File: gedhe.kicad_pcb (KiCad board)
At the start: 2 copper layers, 140 x 120.6 mm, 56 parts, among them SW1 switch, SW10 switch, SW11 switch, SW12 switch, SW13 switch, SW14 switch, SW15 switch, SW16 switch, SW17 switch, SW18 switch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

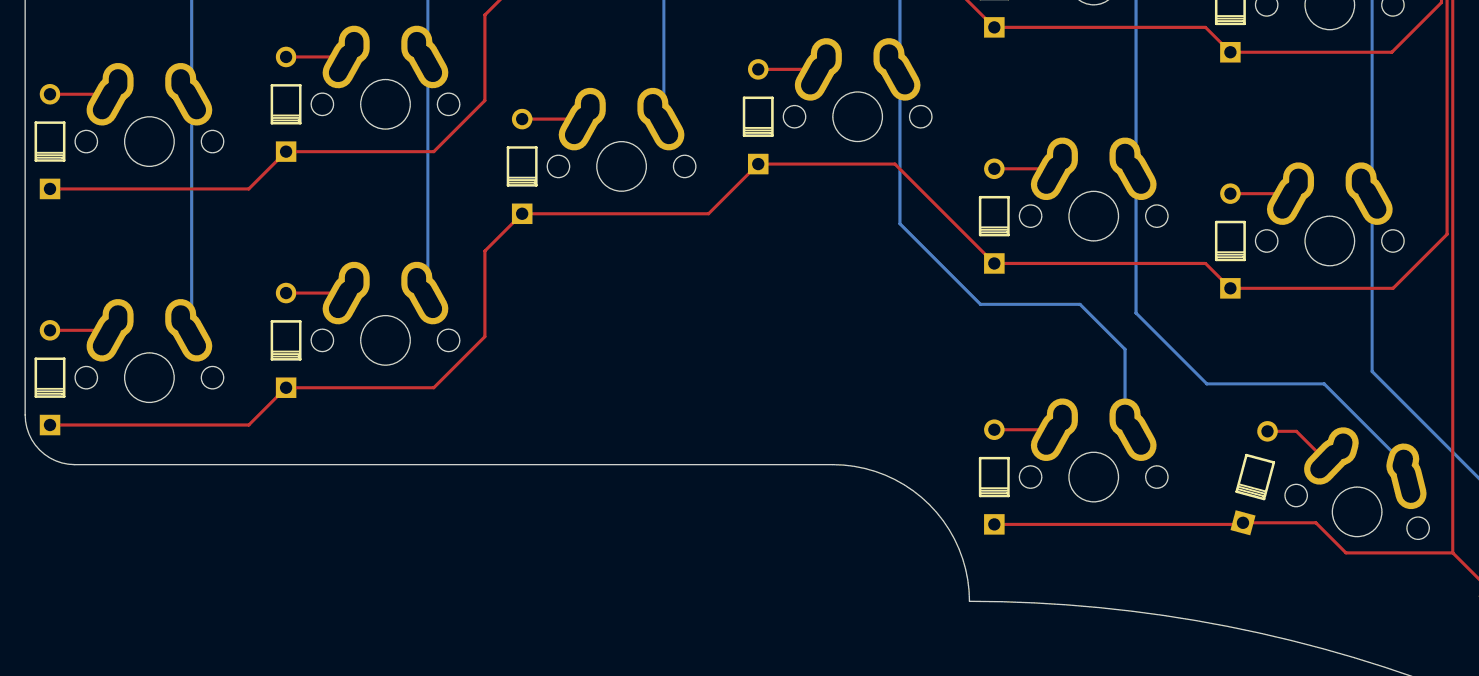
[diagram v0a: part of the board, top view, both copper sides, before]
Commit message: 29 keys per side.
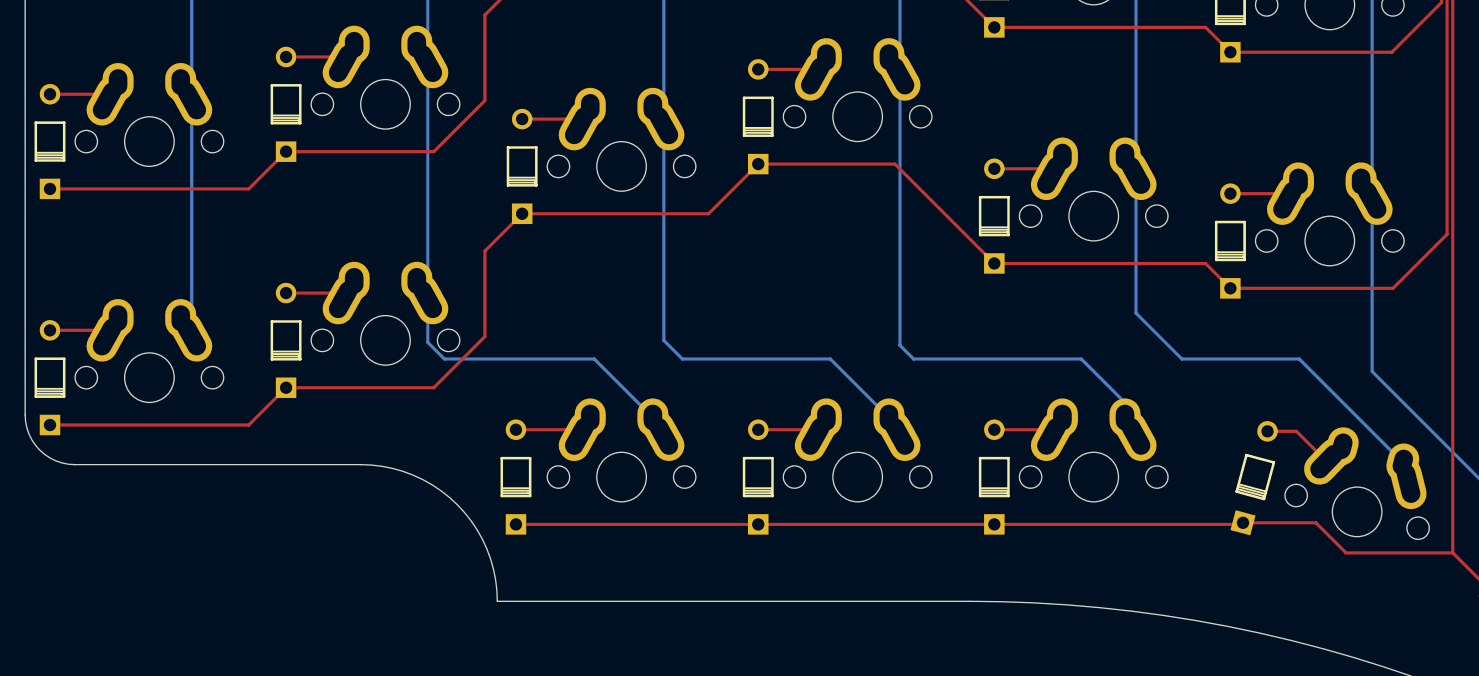
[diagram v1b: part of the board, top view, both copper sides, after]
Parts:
- added D28: D, footprints:diode, F.Cu at (62.5, 117.0)
- added D29: D, footprints:diode, F.Cu at (82.0, 117.0)
- added SW28: switch, footprints:1u-dual, F.Cu at (71.0, 117.0)
- added SW29: switch, footprints:1u-dual, F.Cu at (90.0, 117.0)
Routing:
- net ROW4: track 103.5 -> 142.0 mm
- net COL2: track 183.5 -> 221.4 mm
- net COL1: track 214.6 -> 238.6 mm
- net Net-(D28-Pad2): track 0.00 -> 5.32 mm
- net Net-(D29-Pad2): track 0.00 -> 4.82 mm
- net COL3: track 197.5 -> 200.7 mm
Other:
- outline, holes or cut-outs redrawn

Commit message: added key.
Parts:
- added D30: D, footprints:diode, F.Cu at (62.5, 117.0)
- added SW30: switch, footprints:1u-dual, F.Cu at (71.0, 117.0)
- moved SW27 24.0 mm to (149.0, 104.0), turned to 0 degrees
- moved D22 21.8 mm to (143.0, 123.0), turned to 240 degrees
- moved SW22 21.4 mm to (150.0, 128.0), turned to 330 degrees
- moved SW17 21.4 mm to (130.2, 119.8), turned to 345 degrees
- moved D17 21.0 mm to (122.0, 117.0), turned to 255 degrees
- moved D27 19.5 mm to (141.0, 103.6), turned to 270 degrees
- moved D28 19.5 mm to (82.0, 117.0)
- moved D29 19.0 mm to (101.0, 117.0)
- moved SW28 19.0 mm to (90.0, 117.0)
- moved SW29 19.0 mm to (109.0, 117.0)
- moved U2 6.00 mm to (163.0, 80.0)
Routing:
- net COL0: track 236.7 -> 280.1 mm
- net COL4: track 172.8 -> 200.8 mm
- net COL5: track 158.3 -> 135.6 mm
- net COL3: track 200.7 -> 222.7 mm
- net COL1: track 238.6 -> 259.3 mm
- net COL2: track 221.4 -> 241.0 mm
- net Net-(U1-Pad21): track 46.9 -> 40.9 mm
- net Net-(U1-Pad23): track 53.4 -> 47.4 mm
- net SDA: track 47.9 -> 41.9 mm
- net Net-(D30-Pad2): track 0.00 -> 5.32 mm
- net ROW4: track 142.0 -> 146.0 mm
- net Net-(D17-Pad2): track 4.82 -> 5.78 mm
- net Net-(D28-Pad2): track 5.32 -> 4.82 mm

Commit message: additional key wasn't placed correctly.
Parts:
- moved D27 2.24 mm to (140.0, 101.6)
- moved SW27 2.24 mm to (148.0, 102.0)
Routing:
- net COL5: track 135.6 -> 133.7 mm
- net COL1: track 259.3 -> 261.1 mm
- net COL3: track 222.7 -> 224.3 mm
- net COL2: track 241.0 -> 242.6 mm
- net ROW4: track 146.0 -> 144.9 mm
